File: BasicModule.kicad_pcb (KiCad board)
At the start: 2 copper layers, 0 parts

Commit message: Se decide implementar el modulo solo para leds, buzzers y potenciometro
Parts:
- added BZ1: Buzzer, Buzzers_Beepers:Buzzer_12x9.5RM7.6, F.Cu at (137.9, 101.3)
- added C1: C, Capacitors_SMD:C_0805, F.Cu at (195.9, 108.0)
- added D1: LED, LEDs:LED-5MM, F.Cu at (166.1, 102.1)
- added P1: CONN_01X03, Connectors_JST:JST_PH_S3B-PH-K_03x2.00mm_Angled, F.Cu at (167.6, 126.6)
- added Q1: Q_NPN_BCE, TO_SOT_Packages_SMD:SOT-23, F.Cu at (152.6, 129.2)
- added R1: R, Resistors_SMD:R_0805, F.Cu at (159.0, 128.8)
- added R2: R, Resistors_SMD:R_0805, F.Cu at (176.5, 131.5)
- added R3: R, Resistors_SMD:R_0805, F.Cu at (199.8, 108.0)
- added R4: R, Resistors_SMD:R_0805, F.Cu at (195.7, 114.4)
- added R5: R, Resistors_SMD:R_0805, F.Cu at (186.0, 121.4)
- added RV1: POT, w_pth_resistors:trimmer_alps-rk09k1130ah1, F.Cu at (152.9, 113.8)
- added SW1: SW_Push_Dual, Buttons_Switches_THT:SW_PUSH-12mm, F.Cu at (154.4, 93.0)

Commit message: LAyout Terminado
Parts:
- removed C1: C, Capacitors_SMD:C_0805
- removed R3, R4, R5: R, Resistors_SMD:R_0805
- removed SW1: SW_Push_Dual, Buttons_Switches_THT:SW_PUSH-12mm
- added M1: LED_PIRANHA_5MM, SparkFun-LED:LED_PIRANHA_5MM, F.Cu at (137.9, 101.3)
- added REF**: MountingHole_3.2mm_M3, Mounting_Holes:MountingHole_3.2mm_M3, F.Cu at (131.3, 96.5)
- added REF**: MountingHole_3.2mm_M3, Mounting_Holes:MountingHole_3.2mm_M3, F.Cu at (144.5, 96.5)
- R1, R2: value R -> 1k
- moved R2 51.7 mm to (131.6, 105.9), turned to 270 degrees
- moved P1 35.1 mm to (135.9, 111.4)
- moved R1 33.6 mm to (131.6, 109.5), turned to 270 degrees
- moved D1 26.9 mm to (139.2, 101.6), turned to 180 degrees
- moved Q1 22.4 mm to (144.3, 108.5), turned to 180 degrees
- moved RV1 19.5 mm to (137.9, 101.3)
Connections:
- P1 pad 3: Net-(P1-Pad3) -> SIGNAL
- Q1 pad 2: Net-(Q1-Pad2) -> Net-(BZ1-Pad1)
- R1 pad 1: +5V -> SIGNAL
- R1 pad 2: Net-(BZ1-Pad2) -> Net-(Q1-Pad1)
- R2 pad 1: Net-(Q1-Pad2) -> Net-(BZ1-Pad2)
- R2 pad 2: Net-(BZ1-Pad1) -> +5V
- RV1 pad 2: Net-(BZ1-Pad1) -> SIGNAL
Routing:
- net Net-(Q1-Pad1): track 0.00 -> 18.3 mm, vias 0 -> 2
- net Net-(BZ1-Pad1): track 0.00 -> 16.6 mm
- net Net-(BZ1-Pad2): track 0.00 -> 16.2 mm
- net SIGNAL: track 0.00 -> 13.7 mm, vias 0 -> 2
- net +5V: track 0.00 -> 9.49 mm
- net GND: track 0.00 -> 9.13 mm
- added copper zone on B.Cu, net GND
- added copper zone on F.Cu, net GND
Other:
- board outline added: 17.8 x 20.3 mm

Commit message: Gerbers exportados
Gerbers exportados para prueba de panelizacion
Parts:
- added G***: LOGO, logos_frizzy:web, B.Cu at (131.3, 108.5)
- added G***: LOGO, logos_frizzy:glance, B.Cu at (143.5, 111.3)

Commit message: Logo cambiado
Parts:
- removed the G*** at (143.5, 111.3)
- added G***: LOGO, BasicModule:logo_blanco, B.Cu at (143.8, 111.3)
- added G***: LOGO, BasicModule:logo_oro, B.Cu at (144.0, 111.6)
- moved G*** 0.71 mm to (130.6, 108.3)

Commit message: añadido nuevo logo
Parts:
- removed the G*** at (143.8, 111.3)
- removed the G*** at (144.0, 111.6)
- added G***: LOGO, Grape:atom_small, B.Cu at (143.8, 111.2)

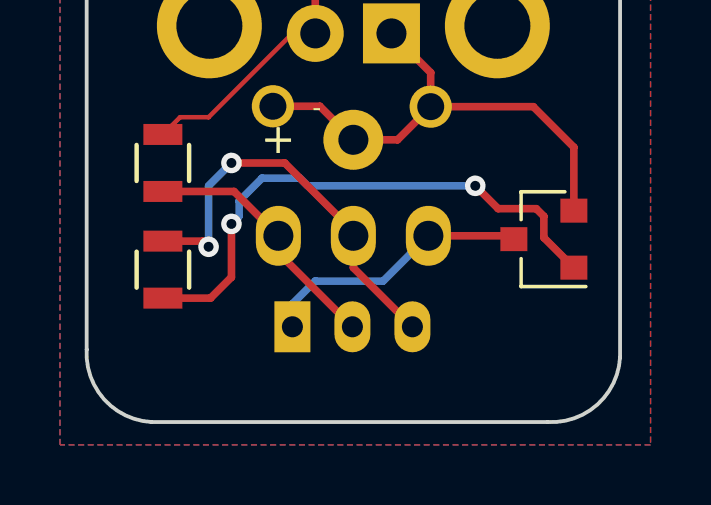
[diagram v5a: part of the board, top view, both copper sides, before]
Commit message: Conector cambiado
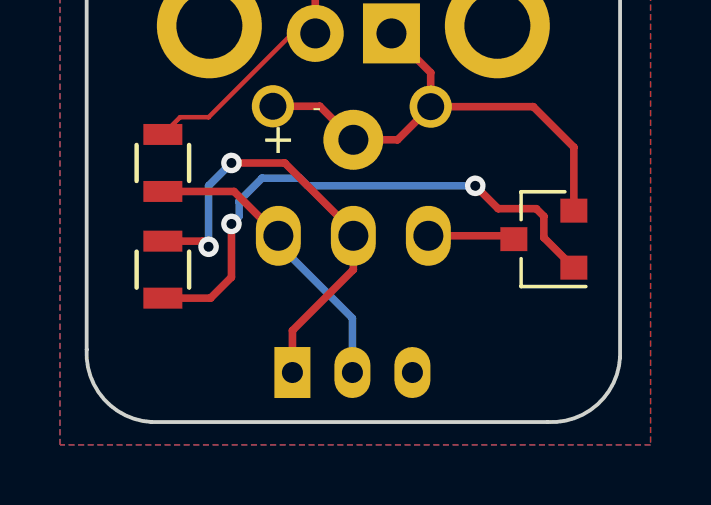
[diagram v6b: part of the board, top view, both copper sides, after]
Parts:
- moved P1 1.52 mm to (135.9, 112.9)
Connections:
- P1 pad 1: GND -> SIGNAL
- P1 pad 3: SIGNAL -> GND
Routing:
- net GND: track 9.13 -> 2.90 mm
- net +5V: track 9.49 -> 11.4 mm
- net SIGNAL: track 13.7 -> 15.3 mm
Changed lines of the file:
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@@
     (thickness 1.6)
     (drawings 11)
-    (tracks 59)
+    (tracks 57)
     (zones 0)
     (modules 12)
@@
   )
   (module Connectors_JST:JST_PH_S3B-PH-K_03x2.00mm_Angled (layer F.Cu)
-    (at 135.89 111.379)
+    (at 135.89 112.903)
     (descr http://www.jst-mfg.com/product/pdf/eng/ePH.pdf)
     (tags "connector jst ph")
@@
     (fp_line (start 6.45 6.75) (end -2.45 6.75) (layer Dwgs.User) (width 0.05))
     (pad 1 thru_hole rect (at 0 0) (size 1.2 1.7) (drill 0.7) (layers *.Cu *.Mask)
-      (net 3 GND))
+      (net 6 SIGNAL))
     (pad 2 thru_hole oval (at 2 0) (size 1.2 1.7) (drill 0.7) (layers *.Cu *.Mask)
       (net 4 +5V))
     (pad 3 thru_hole oval (at 4 0) (size 1.2 1.7) (drill 0.7) (layers *.Cu *.Mask)
-      (net 6 SIGNAL))
+      (net 3 GND))
   )
   (module SparkFun-LED:LED_PIRANHA_5MM (layer F.Cu)
@@
   (segment (start 137.922 97.54616) (end 136.4615 97.54616) (width 0.254) (layer F.Cu) (net 2))
   (segment (start 136.4615 97.54616) (end 135.23468 98.77298) (width 0.254) (layer F.Cu) (net 2))
-  (segment (start 135.89 111.379) (end 135.89 110.617) (width 0.254) (layer B.Cu) (net 3))
-  (segment (start 135.89 110.617) (end 136.652 109.855) (width 0.254) (layer B.Cu) (net 3))
-  (segment (start 136.652 109.855) (end 138.913 109.855) (width 0.254) (layer B.Cu) (net 3))
-  (segment (start 138.913 109.855) (end 140.422 108.346) (width 0.254) (layer B.Cu) (net 3))
   (segment (start 140.422 108.346) (end 143.16 108.346) (width 0.254) (layer F.Cu) (net 3))
   (segment (start 143.16 108.346) (end 143.272 108.458) (width 0.254) (layer F.Cu) (net 3))
+  (segment (start 135.422 108.346) (end 135.422 108.625) (width 0.254) (layer B.Cu) (net 4) (status C00000))
+  (segment (start 135.422 108.625) (end 137.89 111.093) (width 0.254) (layer B.Cu) (net 4) (status 400000))
+  (segment (start 137.89 111.093) (end 137.89 112.903) (width 0.254) (layer B.Cu) (net 4) (status 800000))
   (segment (start 135.422 108.346) (end 135.422 108.911) (width 0.254) (layer F.Cu) (net 4))
-  (segment (start 135.422 108.911) (end 137.89 111.379) (width 0.254) (layer F.Cu) (net 4))
   (segment (start 135.422 108.346) (end 135.422 108.498) (width 0.254) (layer F.Cu) (net 4))
-  (segment (start 138.144 111.22) (end 138.144 111.379) (width 0.254) (layer F.Cu) (net 4))
   (segment (start 131.572 106.868) (end 133.944 106.868) (width 0.254) (layer F.Cu) (net 4))
   (segment (start 133.944 106.868) (end 135.422 108.346) (width 0.254) (layer F.Cu) (net 4))
@@
   (segment (start 133.858 109.728) (end 133.858 107.95) (width 0.254) (layer F.Cu) (net 5))
   (segment (start 133.162 110.424) (end 133.858 109.728) (width 0.254) (layer F.Cu) (net 5))
-  (segment (start 137.922 108.346) (end 137.922 109.411) (width 0.254) (layer F.Cu) (net 6))
-  (segment (start 137.922 109.411) (end 139.89 111.379) (width 0.254) (layer F.Cu) (net 6))
+  (segment (start 137.922 108.346) (end 137.922 109.474) (width 0.254) (layer F.Cu) (net 6) (status 400000))
+  (segment (start 135.89 111.506) (end 135.89 112.903) (width 0.254) (layer F.Cu) (net 6) (status 800000))
+  (segment (start 137.922 109.474) (end 135.89 111.506) (width 0.254) (layer F.Cu) (net 6))
   (segment (start 137.922 108.346) (end 137.922 108.204) (width 0.254) (layer F.Cu) (net 6))
   (segment (start 137.922 108.204) (end 135.636 105.918) (width 0.254) (layer F.Cu) (net 6))
